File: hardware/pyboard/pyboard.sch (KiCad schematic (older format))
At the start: 65 parts, among them J1 Battery, J2 Arduino_Mega2560_Shield, J6 USB_B_Micro, J9 Micro_SD_SCHA5B0200, Q1 IRLML6402, Q2 IRLML6402, SW1 RST, SW2 USR, U1 STM32F405RGT6, U2 MCP1703A-3302_SOT89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

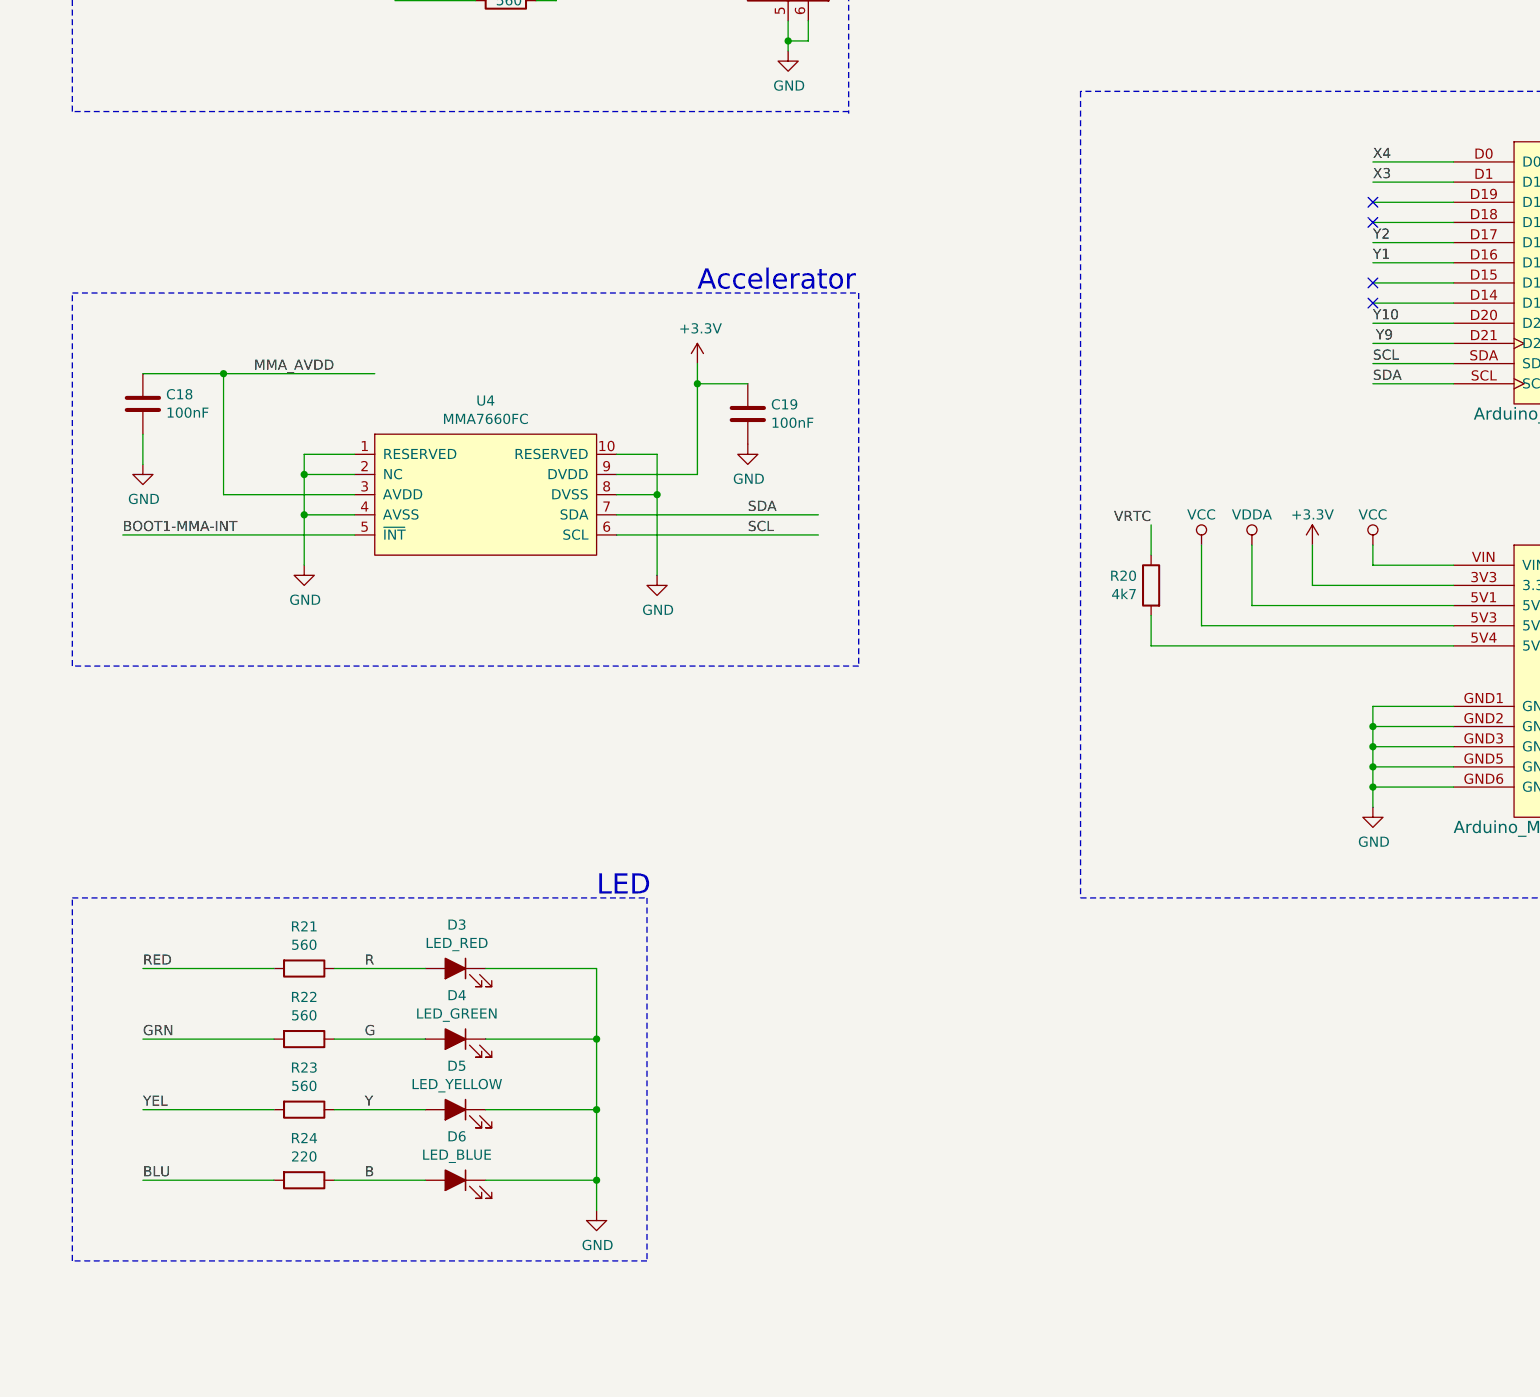
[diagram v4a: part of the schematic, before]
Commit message: Swap Y and X pins
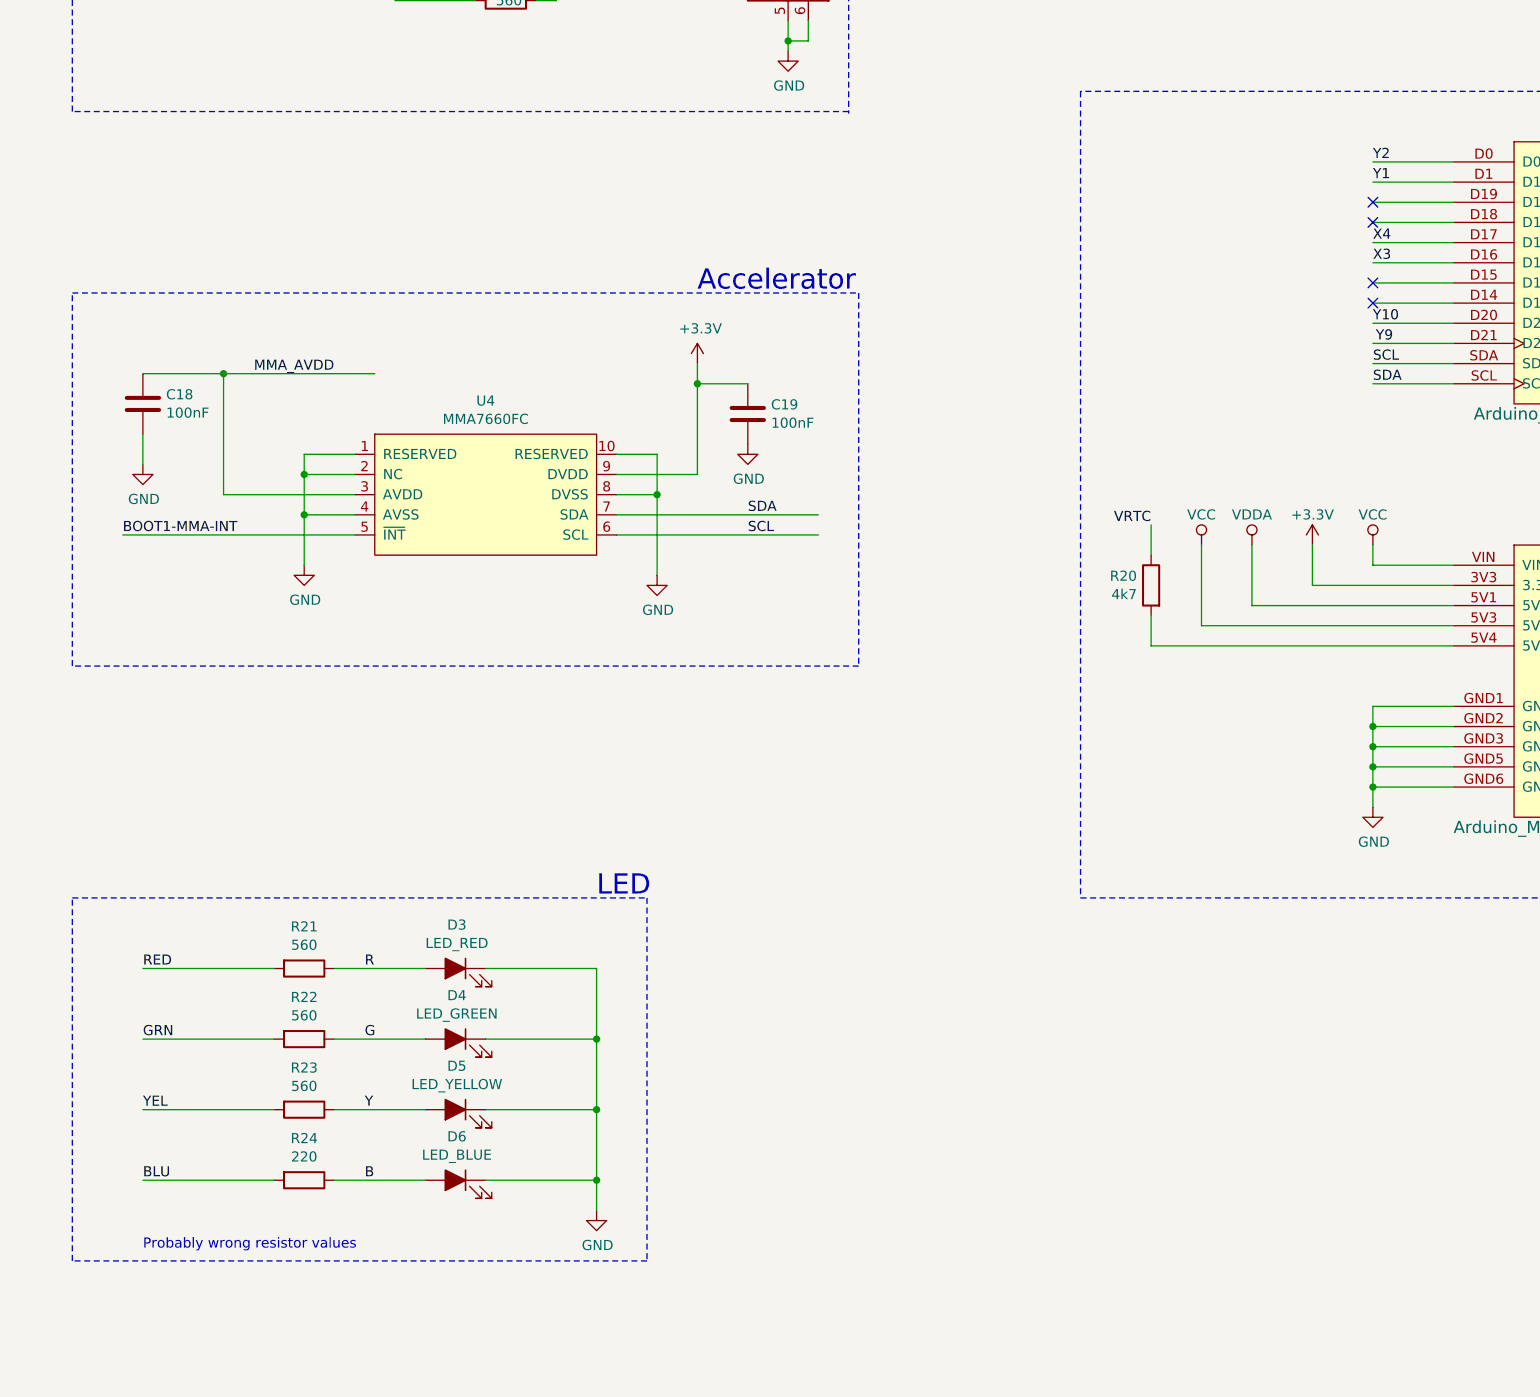
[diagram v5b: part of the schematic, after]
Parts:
- D1, D3, D4, D5, D6: footprint LED_SMD:LED_1206_3216Metric -> LED_SMD:LED_0603_1608Metric
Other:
- note added: "Probably wrong resistor values"
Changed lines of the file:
@@
 EESchema Schematic File Version 4
-LIBS:pyboard-cache
 EELAYER 30 0
 EELAYER END
@@
 Wire Wire Line
 	4700 13150 4700 13250
-Text Label 15450 4850 0    50   ~ 0
+Text Label 15450 4450 0    50   ~ 0
 Y1
-Text Label 15450 4750 0    50   ~ 0
+Text Label 15450 4350 0    50   ~ 0
 Y2
 Text Label 19450 4350 0    50   ~ 0
@@
 Text Label 17450 4450 0    50   ~ 0
 X2
-Text Label 15450 4450 0    50   ~ 0
+Text Label 15450 4850 0    50   ~ 0
 X3
-Text Label 15450 4350 0    50   ~ 0
+Text Label 15450 4750 0    50   ~ 0
 X4
 Wire Wire Line
@@
 F 0 "D3" H 10893 8566 50  0000 C CNN
 F 1 "LED_RED" H 10893 8475 50  0000 C CNN
-F 2 "LED_SMD:LED_1206_3216Metric" H 10900 8350 50  0001 C CNN
-F 3 "~" H 10900 8350 50  0001 C CNN
+F 2 "LED_SMD:LED_0603_1608Metric" H 10900 8350 50  0001 C CNN
+F 3 "https://belchip.by/product/?selected_product=34186" H 10900 8350 50  0001 C CNN
 	1    10900 8350
 	-1   0    0    -1
@@
 F 0 "D4" H 10893 8916 50  0000 C CNN
 F 1 "LED_GREEN" H 10893 8825 50  0000 C CNN
-F 2 "LED_SMD:LED_1206_3216Metric" H 10900 8700 50  0001 C CNN
+F 2 "LED_SMD:LED_0603_1608Metric" H 10900 8700 50  0001 C CNN
 F 3 "~" H 10900 8700 50  0001 C CNN
 	1    10900 8700
@@
 F 0 "D5" H 10893 9266 50  0000 C CNN
 F 1 "LED_YELLOW" H 10893 9175 50  0000 C CNN
-F 2 "LED_SMD:LED_1206_3216Metric" H 10900 9050 50  0001 C CNN
+F 2 "LED_SMD:LED_0603_1608Metric" H 10900 9050 50  0001 C CNN
 F 3 "~" H 10900 9050 50  0001 C CNN
 	1    10900 9050
@@
 F 0 "D6" H 10893 9616 50  0000 C CNN
 F 1 "LED_BLUE" H 10893 9525 50  0000 C CNN
-F 2 "LED_SMD:LED_1206_3216Metric" H 10900 9400 50  0001 C CNN
-F 3 "~" H 10900 9400 50  0001 C CNN
+F 2 "LED_SMD:LED_0603_1608Metric" H 10900 9400 50  0001 C CNN
+F 3 "https://belchip.by/product/?selected_product=12555" H 10900 9400 50  0001 C CNN
 	1    10900 9400
 	-1   0    0    -1
@@
 Wire Wire Line
 	10550 1900 10550 2000
-$Comp
-L Device:LED_ALT D1
-U 1 1 5E3D49BE
-P 10550 1750
-F 0 "D1" V 10589 1633 50  0000 R CNN
-F 1 "OC_RED" V 10498 1633 50  0000 R CNN
-F 2 "LED_SMD:LED_1206_3216Metric" H 10550 1750 50  0001 C CNN
-F 3 "~" H 10550 1750 50  0001 C CNN
-	1    10550 1750
-	0    -1   -1   0
-$EndComp
 $Comp
 L Connector_Generic:Conn_01x02 J1
@@
 Text Label 11850 3450 0    50   ~ 0
 ID_USB
+$Comp
+L Device:LED_ALT D1
+U 1 1 5E3D49BE
+P 10550 1750
+F 0 "D1" V 10589 1633 50  0000 R CNN
+F 1 "OC_RED" V 10498 1633 50  0000 R CNN
+F 2 "LED_SMD:LED_0603_1608Metric" H 10550 1750 50  0001 C CNN
+F 3 "~" H 10550 1750 50  0001 C CNN
+	1    10550 1750
+	0    -1   -1   0
+$EndComp
+Text Notes 9350 9750 0    50   ~ 0
+Probably wrong resistor values
 $EndSCHEMATC

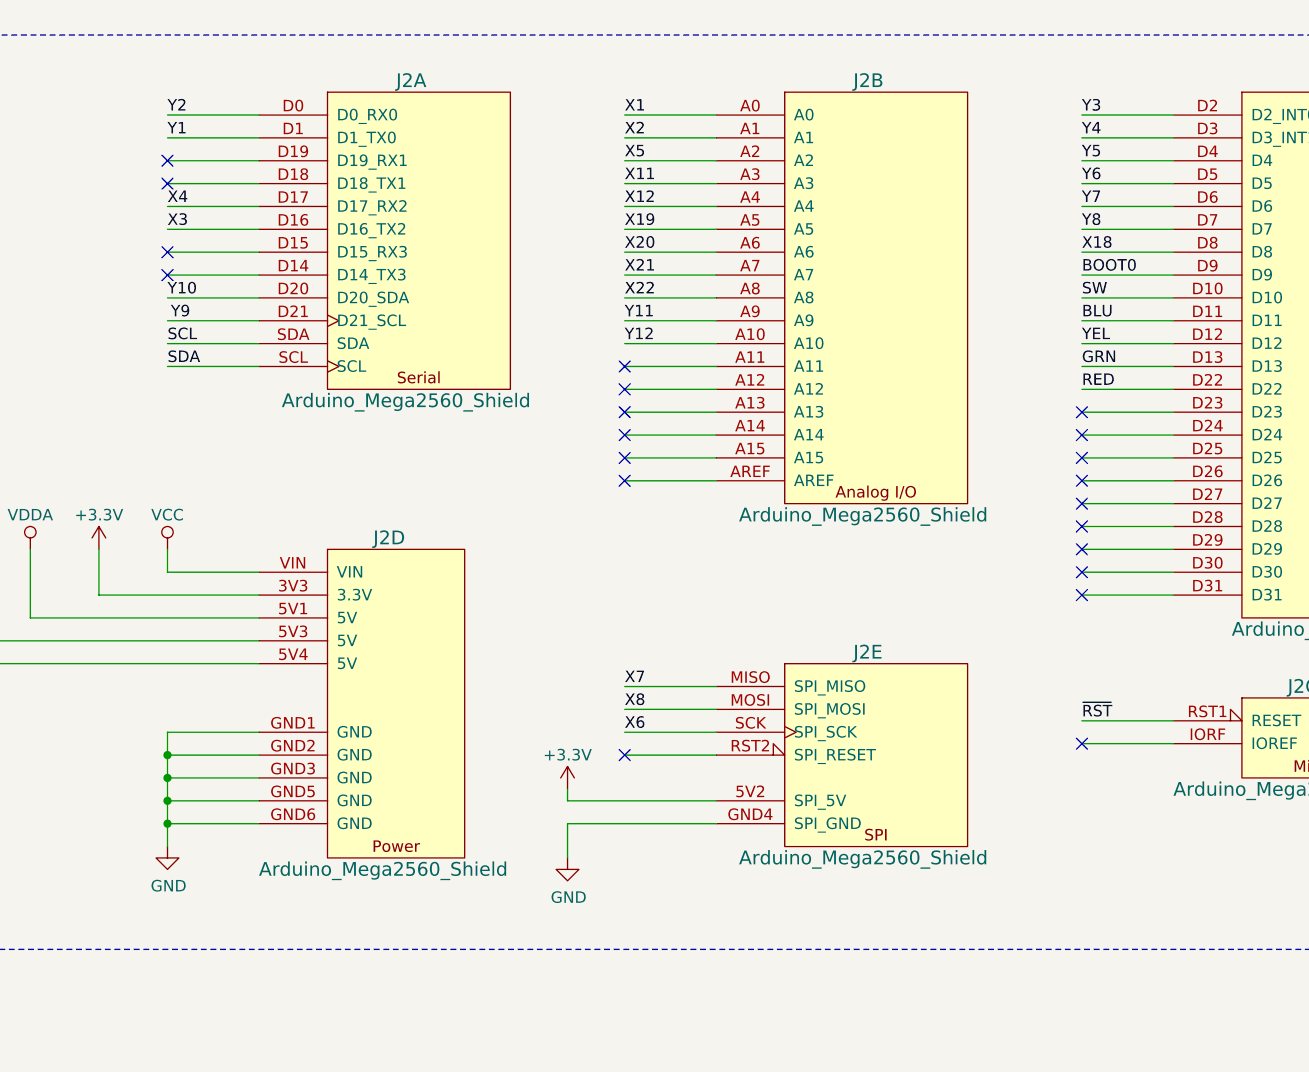
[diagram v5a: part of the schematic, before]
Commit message: Remove ISP pin header
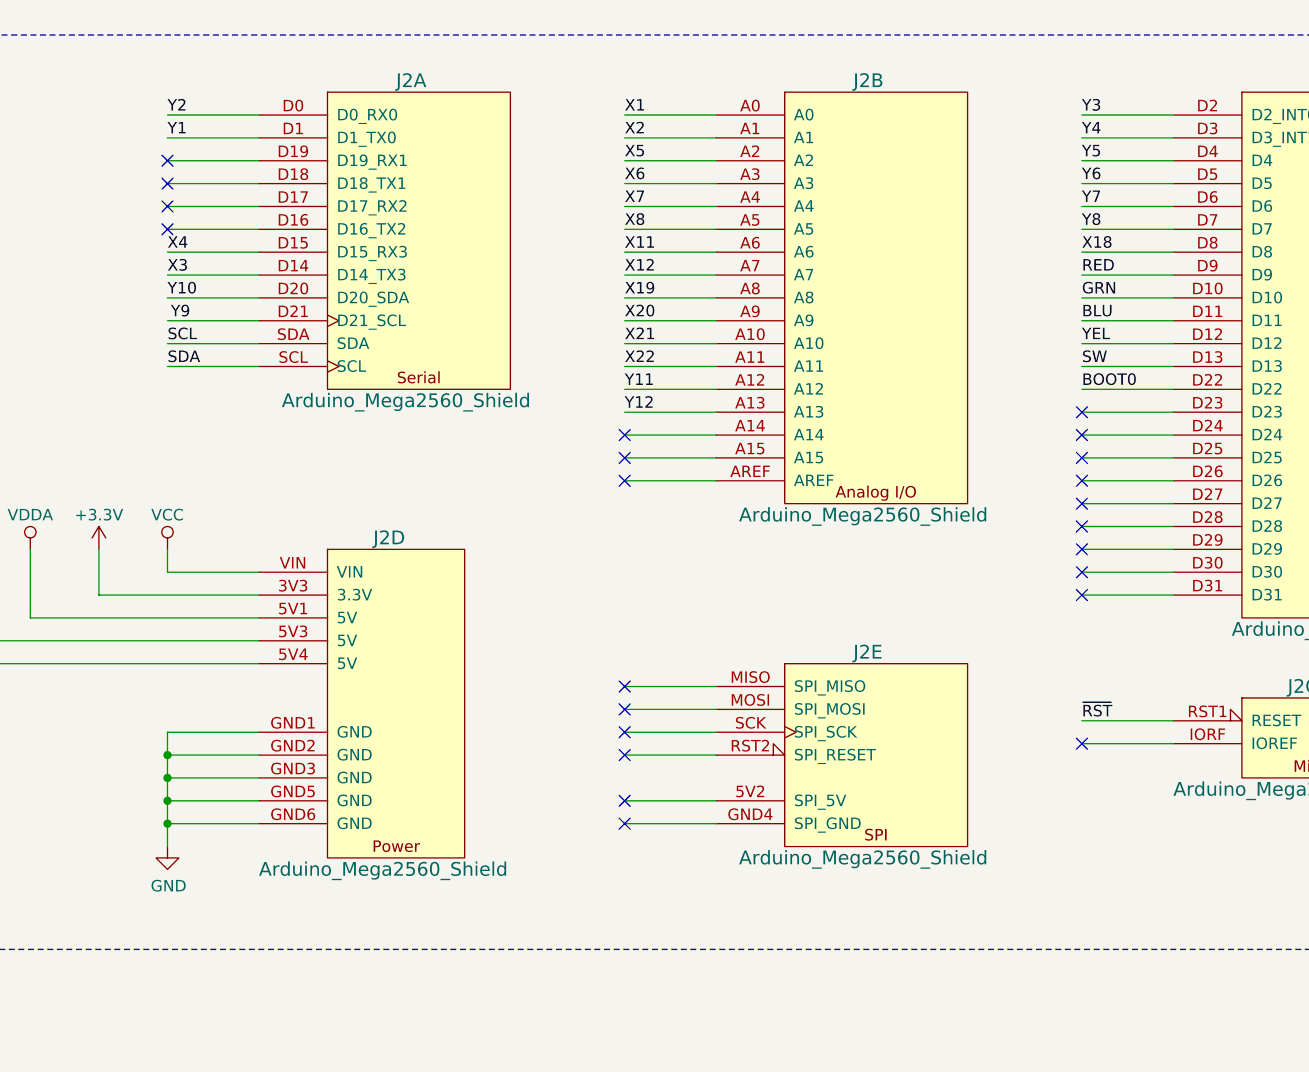
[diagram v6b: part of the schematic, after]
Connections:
- wire segments 377 -> 375
- no-connect marks 43 -> 45
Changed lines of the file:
@@
 EESchema Schematic File Version 4
+LIBS:pyboard-cache
 EELAYER 30 0
 EELAYER END
@@
 Text Label 19450 4850 0    50   ~ 0
 Y8
-Text Label 15450 5350 0    50   ~ 0
-SCL
-Text Label 15450 5450 0    50   ~ 0
-SDA
-Text Label 17450 4650 0    50   ~ 0
+Text Label 17450 4950 0    50   ~ 0
 X11
-Text Label 17450 4750 0    50   ~ 0
+Text Label 17450 5050 0    50   ~ 0
 X12
-Text Label 19450 5050 0    50   ~ 0
+Text Label 19450 5550 0    50   ~ 0
 BOOT0
-Text Label 19450 5150 0    50   ~ 0
+Text Label 19450 5450 0    50   ~ 0
 SW
-Text Label 17450 4950 0    50   ~ 0
+Text Label 17450 5250 0    50   ~ 0
 X20
-Text Label 17450 5050 0    50   ~ 0
+Text Label 17450 5350 0    50   ~ 0
 X21
-Text Label 17450 5150 0    50   ~ 0
+Text Label 17450 5450 0    50   ~ 0
 X22
 Wire Wire Line
@@
 Wire Wire Line
 	4700 13150 5450 13150
-Text Label 17450 5350 0    50   ~ 0
+Text Label 17450 5650 0    50   ~ 0
 Y12
 Text Label 15550 5250 2    50   ~ 0
@@
 Text Label 17450 4450 0    50   ~ 0
 X2
-Text Label 15450 4850 0    50   ~ 0
+Text Label 15450 5050 0    50   ~ 0
 X3
-Text Label 15450 4750 0    50   ~ 0
-X4
 Wire Wire Line
 	6250 1400 6250 1550
@@
 Text Label 15450 5150 0    50   ~ 0
 Y10
-Text Label 17450 5250 0    50   ~ 0
+Text Label 17450 5550 0    50   ~ 0
 Y11
 Text Label 17450 4550 0    50   ~ 0
@@
 	17850 5950 17450 5950
 Wire Wire Line
+	17850 5550 17450 5550
+Wire Wire Line
+	17850 5450 17450 5450
+Wire Wire Line
 	17850 5250 17450 5250
 Wire Wire Line
 	17850 5150 17450 5150
 Wire Wire Line
+	17850 5050 17450 5050
+Wire Wire Line
 	17850 4950 17450 4950
 Wire Wire Line
-	17850 4850 17450 4850
-Wire Wire Line
-	17850 4750 17450 4750
-Wire Wire Line
-	17850 4650 17450 4650
-Wire Wire Line
 	17850 4550 17450 4550
 Wire Wire Line
@@
 Wire Wire Line
 	17850 5650 17450 5650
-Wire Wire Line
-	17850 5550 17450 5550
-Wire Wire Line
-	17850 5450 17450 5450
-Wire Wire Line
-	17850 5350 17450 5350
 Wire Wire Line
 	17850 4450 17450 4450
@@
 $EndComp
 Wire Wire Line
-	17850 5050 17450 5050
-Text Label 17450 4850 0    50   ~ 0
+	17850 5350 17450 5350
+Text Label 17450 5150 0    50   ~ 0
 X19
 Text Label 19450 4950 0    50   ~ 0
@@
 Text Label 19450 5350 0    50   ~ 0
 YEL
-Text Label 19450 5450 0    50   ~ 0
+Text Label 19450 5150 0    50   ~ 0
 GRN
-Text Label 19450 5550 0    50   ~ 0
+Text Label 19450 5050 0    50   ~ 0
 RED
 Wire Wire Line
@@
 Wire Wire Line
 	17850 7150 17450 7150
-Wire Wire Line
-	17850 7050 17450 7050
-Wire Wire Line
-	17850 6950 17450 6950
-Wire Wire Line
-	17850 6850 17450 6850
 $Comp
 L components:Arduino_Mega2560_Shield J2
@@
 	1    0    0    -1
 $EndComp
-Text Label 17450 6950 0    50   ~ 0
-X8
-Text Label 17450 6850 0    50   ~ 0
-X7
-Text Label 17450 7050 0    50   ~ 0
-X6
 $Comp
 L components:Arduino_Mega2560_Shield J2
@@
 NoConn ~ 15450 4550
 NoConn ~ 15450 4650
-NoConn ~ 15450 4950
-NoConn ~ 15450 5050
 Wire Wire Line
 	15850 5250 15450 5250
 NoConn ~ 17450 7150
-NoConn ~ 17450 5450
-NoConn ~ 17450 5550
-NoConn ~ 17450 5650
 NoConn ~ 17450 5750
 NoConn ~ 17450 5850
@@
 	19850 5750 19450 5750
 NoConn ~ 19450 5750
-$Comp
-L power:GND #PWR041
-U 1 1 6093DD55
-P 17200 7600
-F 0 "#PWR041" H 17200 7350 50  0001 C CNN
-F 1 "GND" H 17205 7427 50  0000 C CNN
-F 2 "" H 17200 7600 50  0001 C CNN
-F 3 "" H 17200 7600 50  0001 C CNN
-	1    17200 7600
-	1    0    0    -1
-$EndComp
-Wire Wire Line
-	17200 7450 17200 7600
-$Comp
-L power:+3.3V #PWR040
-U 1 1 60A1EB17
-P 17200 7300
-F 0 "#PWR040" H 17200 7150 50  0001 C CNN
-F 1 "+3.3V" H 17200 7450 50  0000 C CNN
-F 2 "" H 17200 7300 50  0001 C CNN
-F 3 "" H 17200 7300 50  0001 C CNN
-	1    17200 7300
-	1    0    0    -1
-$EndComp
-Wire Wire Line
-	17200 7450 17850 7450
-Wire Wire Line
-	17200 7350 17200 7300
-Wire Wire Line
-	17200 7350 17850 7350
 Wire Notes Line
 	22100 4000 14000 4000
@@
 Text Notes 9350 9750 0    50   ~ 0
 Probably wrong resistor values
+Text Label 15450 5450 0    50   ~ 0
+SDA
+Text Label 15450 5350 0    50   ~ 0
+SCL
+Wire Wire Line
+	17850 7450 17450 7450
+Wire Wire Line
+	17850 7350 17450 7350
+Wire Wire Line
+	17850 6950 17450 6950
+Wire Wire Line
+	17850 6850 17450 6850
+Wire Wire Line
+	17850 7050 17450 7050
+NoConn ~ 17450 6850
+NoConn ~ 17450 6950
+NoConn ~ 17450 7050
+NoConn ~ 17450 7350
+NoConn ~ 17450 7450
+Text Label 15450 4950 0    50   ~ 0
+X4
+Wire Wire Line
+	17850 4850 17450 4850
+Wire Wire Line
+	17850 4750 17450 4750
+Wire Wire Line
+	17850 4650 17450 4650
+Text Label 17450 4650 0    50   ~ 0
+X6
+Text Label 17450 4750 0    50   ~ 0
+X7
+Text Label 17450 4850 0    50   ~ 0
+X8
+NoConn ~ 15450 4750
+NoConn ~ 15450 4850
 $EndSCHEMATC
